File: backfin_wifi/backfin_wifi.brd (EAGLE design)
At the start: 160 x 100 mm, 22 parts

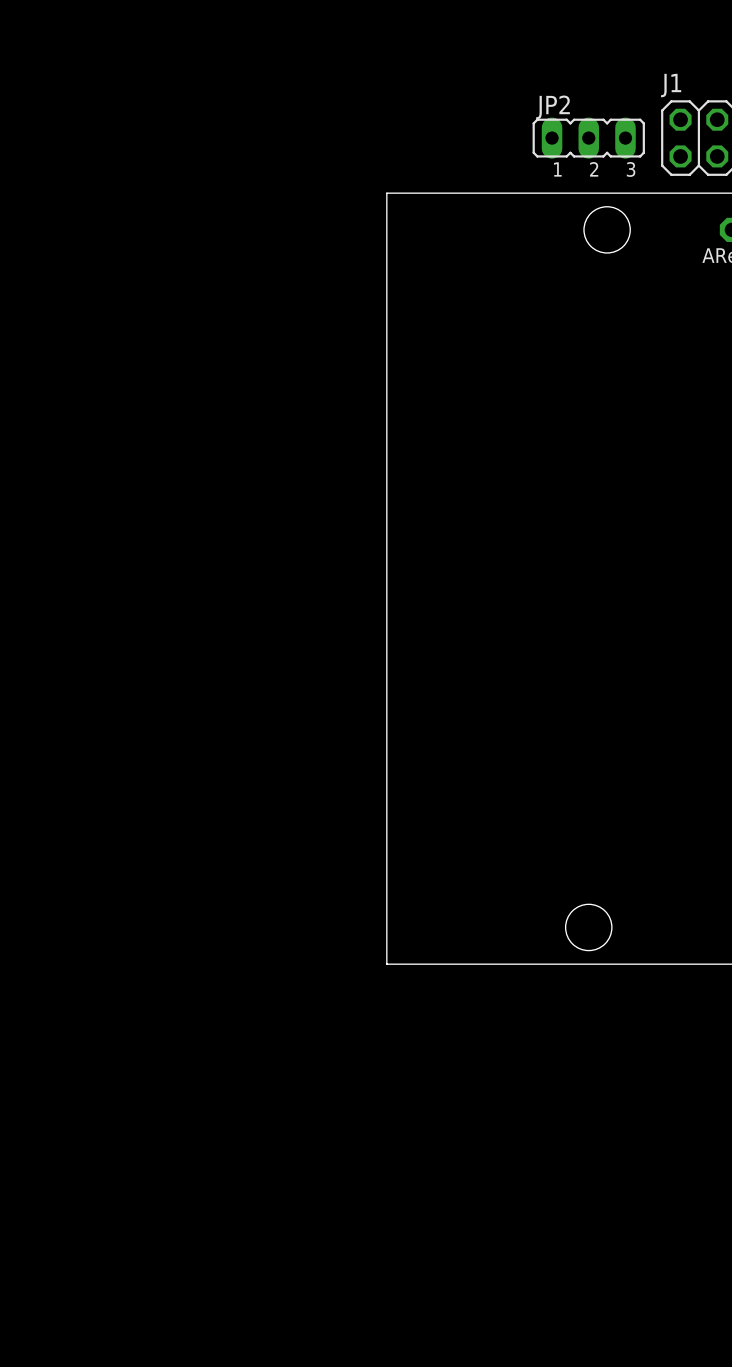
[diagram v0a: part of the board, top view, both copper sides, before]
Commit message: Added push button and LED
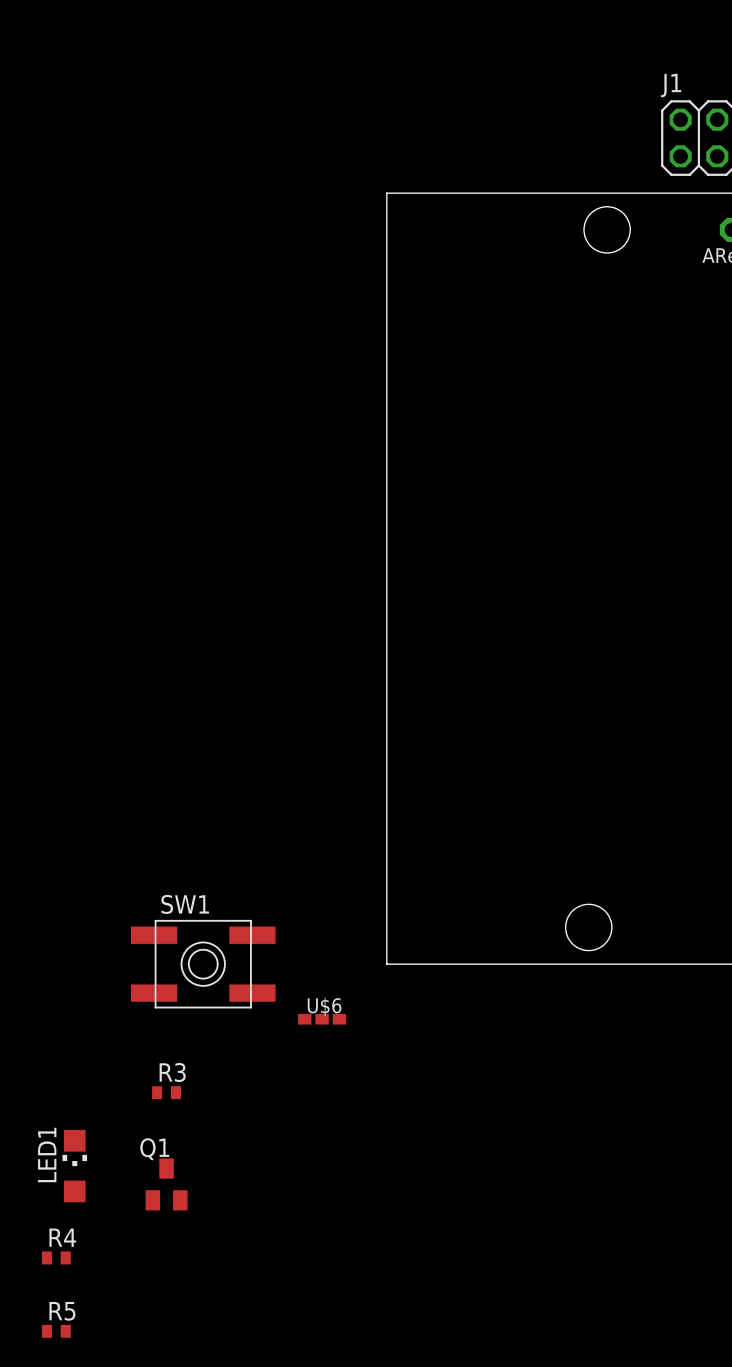
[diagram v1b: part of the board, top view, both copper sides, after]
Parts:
- removed JP2: (no value), jumper:JP2
- added LED1: (no value), adafruit:CHIPLED_1206
- added Q1: (no value), adafruit:SOT23
- added R3, R4: 330, resistor:R1005
- added R5: 0, resistor:R1005
- added SW1: SPST_TACT-EVQQ2, adafruit:EVQ-Q2
- added U$6: 0OHM_JMPR, custom:0OHM_JMPR_0402
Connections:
- new net N$17: R3.1, U$2.D7
- new net N$18: R3.2, SW1.B'
- new net N$19: R5.1, U$2.D6
- new net N$20: LED1.C, Q1.2
- new net N$21: LED1.A, R4.2
- new net N$22: Q1.1, R5.2
- new net SPI_IRQ_HOST: U$2.D9
- net GND: now also Q1.3, SW1.A'; no longer JP2.1
- net N$1: no longer JP2.2
- net N$2: no longer JP2.3
- net SPI_CLK_HOST: now also U$2.D13
- net SPI_CS_HOST: now also U$2.D10
- net SPI_DIN_HOST: now also U$2.D11
- net SPI_DOUT_HOST: now also U$2.D12
- net VBAT_SW_EN: now also U$2.D8
- net VCC: now also R4.1
